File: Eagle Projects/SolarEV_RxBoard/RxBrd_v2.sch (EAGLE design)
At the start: 49 parts, among them U2 ATMEGA32U4-XUAU, X1 USBPTH, X2 5566-6, Y2 16MHz

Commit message: fixed up patels board :D
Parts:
- removed S1: RESET, SparkFun:TAC_SWITCHSMD
- added C10, C11: 100n, resistor:C-USC0805
- added R13, R14, R15, R16: 1k, resistor:R-US_R0805
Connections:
- removed net N$23: ICSP.5, S3.1, S3.2
- new net N$15: R15.1, X2-5.S
- new net RST: ICSP.5, R6.1, S3.1, S3.2, U2.RESET
- net GND: now also C10.2, C11.2, R14.2, R16.2; no longer S1.1, S1.2
- net N$1: now also C11.1, R15.2, R16.1; no longer X2-5.S
- net N$4: now also R13.1; no longer D5.A, D6.C, U2.(PCINT6/OC1B/OC4B/ADC13)PB6
- net N$5: now also C10.1, D5.A, D6.C, R13.2, R14.1, U2.(PCINT6/OC1B/OC4B/ADC13)PB6; no longer R6.1, S1.3, S1.4, U2.RESET
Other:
- moved on the sheet: X2-3, X2-5

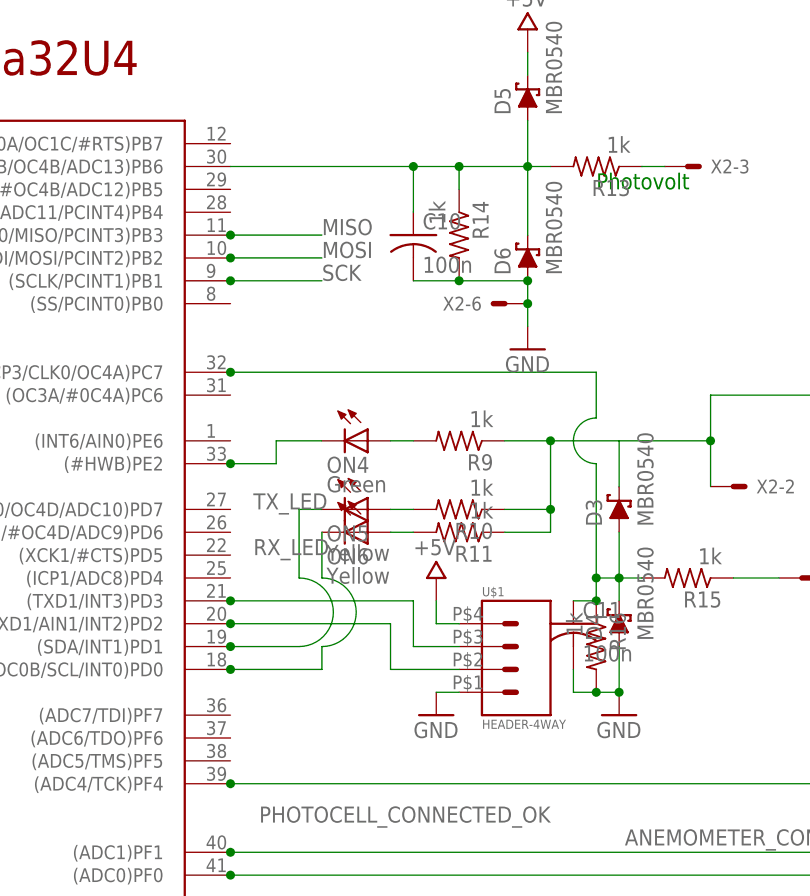
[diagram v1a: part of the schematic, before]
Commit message: final rx board (i think) is still called rev2 xD
on other side, minor software tweaks but they're nonfunctional atm
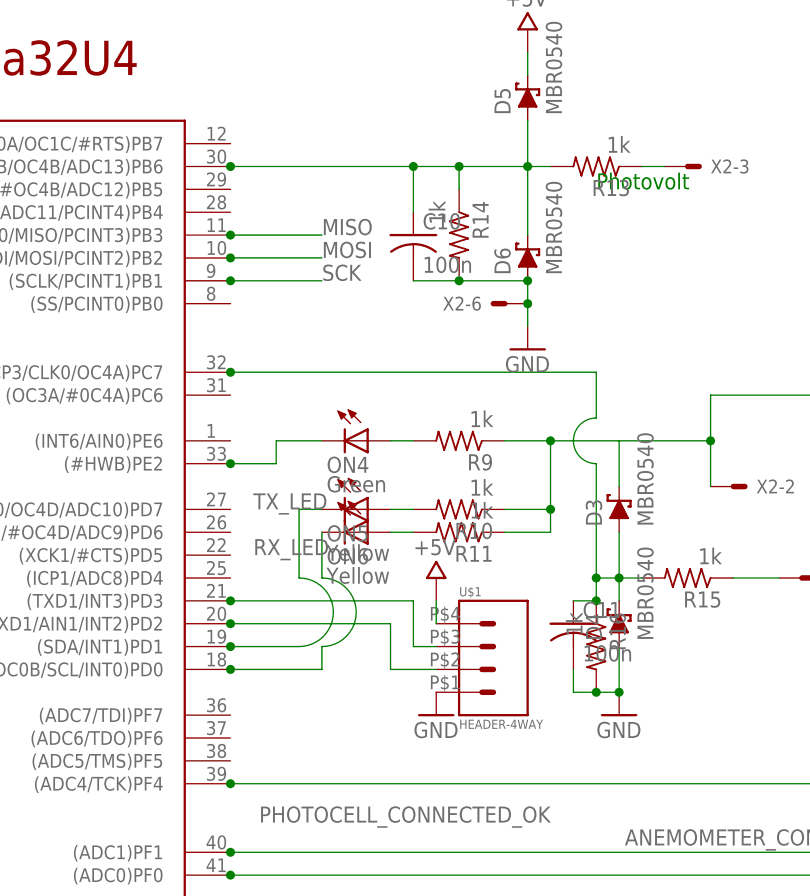
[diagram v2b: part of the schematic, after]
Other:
- moved on the sheet: U$1
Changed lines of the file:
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@@
 <?xml version="1.0" encoding="utf-8"?>
 <!DOCTYPE eagle SYSTEM "eagle.dtd">
-<eagle version="7.2.0">
+<eagle version="7.1.0">
 <drawing>
 <settings>
@@
 <instance part="X2" gate="-6" x="182.88" y="-40.64" rot="R180"/>
 <instance part="JP1" gate="A" x="27.94" y="-30.48"/>
-<instance part="U$1" gate="G$1" x="182.88" y="-78.74"/>
+<instance part="U$1" gate="G$1" x="180.34" y="-78.74"/>
 <instance part="U$3" gate="G$1" x="175.26" y="-71.12"/>
 <instance part="GND10" gate="1" x="175.26" y="-86.36"/>
@@
 <pinref part="U$1" gate="G$1" pin="P$4"/>
 <pinref part="U$3" gate="G$1" pin="+5V"/>
-<wire x1="177.8" y1="-76.2" x2="175.26" y2="-76.2" width="0.1524" layer="91"/>
 <wire x1="175.26" y1="-76.2" x2="175.26" y2="-73.66" width="0.1524" layer="91"/>
 </segment>
@@
 <pinref part="U$1" gate="G$1" pin="P$1"/>
 <pinref part="GND10" gate="1" pin="GND"/>
-<wire x1="177.8" y1="-83.82" x2="175.26" y2="-83.82" width="0.1524" layer="91"/>
 </segment>
 </net>
@@
 <wire x1="170.18" y1="-76.2" x2="170.18" y2="-81.28" width="0.1524" layer="91"/>
 <pinref part="U$1" gate="G$1" pin="P$2"/>
-<wire x1="170.18" y1="-81.28" x2="177.8" y2="-81.28" width="0.1524" layer="91"/>
+<wire x1="170.18" y1="-81.28" x2="175.26" y2="-81.28" width="0.1524" layer="91"/>
 </segment>
 </net>
@@
 <junction x="152.4" y="-73.66"/>
 <pinref part="U$1" gate="G$1" pin="P$3"/>
-<wire x1="177.8" y1="-78.74" x2="172.72" y2="-78.74" width="0.1524" layer="91"/>
+<wire x1="175.26" y1="-78.74" x2="172.72" y2="-78.74" width="0.1524" layer="91"/>
 <wire x1="172.72" y1="-78.74" x2="172.72" y2="-73.66" width="0.1524" layer="91"/>
 </segment>
@@
 <wire x1="172.72" y1="-25.4" x2="172.72" y2="-30.48" width="0.1524" layer="91"/>
 <junction x="172.72" y="-25.4"/>
-</segment>
-</net>
+<junction x="152.4" y="-25.4"/>
+</segment>
+</net>

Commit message: Potato!
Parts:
- removed ICSP: ICSP, SmartPrj:PINHD-2X3
- added Q2: (no value), crystal:CRYSTALHC49S
- JP1: value (none) -> AVR-ISP6-75869-131; device jumper:JP1E -> atmel-avr:AVR-ISP6-75869-131
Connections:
- net GND: now also JP1.6; no longer ICSP.6
- net MISO: now also JP1.1; no longer ICSP.1
- net MOSI: now also JP1.4; no longer ICSP.4
- net N$10: now also JP1.2; no longer ICSP.2
- net RST: now also JP1.5; no longer ICSP.5
- net SCK: now also JP1.3; no longer ICSP.3
- net XTAL1: now also Q2.1
- net XTAL2: now also Q2.2
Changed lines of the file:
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@@
 <?xml version="1.0" encoding="utf-8"?>
 <!DOCTYPE eagle SYSTEM "eagle.dtd">
-<eagle version="7.1.0">
+<eagle version="7.2.0">
 <drawing>
 <settings>
@@
 </classes>
 <parts>
-<part name="ICSP" library="SmartPrj" deviceset="PINHD-2X3" device="" value="ICSP"/>
 <part name="P+1" library="supply1" deviceset="+5V" device=""/>
 <part name="GND12" library="supply1" deviceset="GND" device=""/>
@@
 <part name="X1" library="SparkFun" deviceset="USB" device="PTH"/>
 <part name="X2" library="con-molex" deviceset="5566-6" device=""/>
-<part name="JP1" library="jumper" deviceset="JP1E" device=""/>
 <part name="U$1" library="con-TE-EP" deviceset="HEADER-4WAY" device=""/>
 <part name="U$3" library="MyPOW" deviceset="+5V" device=""/>
@@
 <part name="R16" library="resistor" deviceset="R-US_" device="R0805" value="1k"/>
 <part name="C11" library="resistor" deviceset="C-US" device="C0805" value="100n"/>
+<part name="Q2" library="crystal" deviceset="CRYSTAL" device="HC49S"/>
+<part name="JP1" library="atmel-avr" deviceset="AVR-ISP6-" device="75869-131"/>
 </parts>
 <sheets>
@@
 </plain>
 <instances>
-<instance part="ICSP" gate="A" x="71.12" y="-96.52" smashed="yes">
-<attribute name="NAME" x="64.77" y="-90.805" size="1.778" layer="95"/>
-<attribute name="VALUE" x="74.93" y="-91.44" size="1.778" layer="96"/>
-</instance>
 <instance part="P+1" gate="1" x="86.36" y="-83.82" smashed="yes">
 <attribute name="VALUE" x="88.265" y="-81.28" size="1.778" layer="96" rot="R180"/>
@@
 <instance part="X2" gate="-5" x="215.9" y="-71.12"/>
 <instance part="X2" gate="-6" x="182.88" y="-40.64" rot="R180"/>
-<instance part="JP1" gate="A" x="27.94" y="-30.48"/>
 <instance part="U$1" gate="G$1" x="180.34" y="-78.74"/>
 <instance part="U$3" gate="G$1" x="175.26" y="-71.12"/>
@@
 <instance part="R16" gate="G$1" x="193.04" y="-78.74" rot="R270"/>
 <instance part="C11" gate="G$1" x="190.5" y="-76.2"/>
+<instance part="Q2" gate="G$1" x="71.12" y="-33.02" rot="R90"/>
+<instance part="JP1" gate="G$1" x="78.74" y="-134.62" rot="R90"/>
 </instances>
 <busses>
@@
 <segment>
 <wire x1="86.36" y1="-99.06" x2="76.2" y2="-99.06" width="0.1524" layer="91"/>
-<pinref part="ICSP" gate="A" pin="6"/>
 <pinref part="GND1" gate="1" pin="GND"/>
-<junction x="76.2" y="-99.06"/>
 </segment>
 <segment>
@@
 <pinref part="GND10" gate="1" pin="GND"/>
 </segment>
+<segment>
+<pinref part="JP1" gate="G$1" pin="6"/>
+<wire x1="86.36" y1="-127" x2="86.36" y2="-116.84" width="0.1524" layer="91"/>
+<label x="86.36" y="-116.84" size="1.778" layer="95" rot="R90"/>
+</segment>
 </net>
 <net name="AREF" class="4">
@@
 <wire x1="68.58" y1="-96.52" x2="58.42" y2="-96.52" width="0.1524" layer="91"/>
 <label x="53.34" y="-96.52" size="1.778" layer="95"/>
-<pinref part="ICSP" gate="A" pin="3"/>
-<junction x="68.58" y="-96.52"/>
+</segment>
+<segment>
+<pinref part="JP1" gate="G$1" pin="3"/>
+<wire x1="78.74" y1="-127" x2="78.74" y2="-116.84" width="0.1524" layer="91"/>
+<label x="78.74" y="-116.84" size="1.778" layer="95" rot="R90"/>
 </segment>
 </net>
@@
 <wire x1="68.58" y1="-93.98" x2="60.96" y2="-93.98" width="0.1524" layer="91"/>
 <label x="55.88" y="-93.98" size="1.778" layer="95"/>
-<pinref part="ICSP" gate="A" pin="1"/>
-<junction x="68.58" y="-93.98"/>
+</segment>
+<segment>
+<pinref part="JP1" gate="G$1" pin="1"/>
+<wire x1="73.66" y1="-127" x2="73.66" y2="-116.84" width="0.1524" layer="91"/>
+<label x="73.66" y="-116.84" size="1.778" layer="95" rot="R90"/>
 </segment>
 </net>
@@
 <wire x1="76.2" y1="-96.52" x2="86.36" y2="-96.52" width="0.1524" layer="91"/>
 <label x="81.28" y="-96.52" size="1.778" layer="95"/>
-<pinref part="ICSP" gate="A" pin="4"/>
-<junction x="76.2" y="-96.52"/>
+</segment>
+<segment>
+<pinref part="JP1" gate="G$1" pin="4"/>
+<wire x1="81.28" y1="-127" x2="81.28" y2="-116.84" width="0.1524" layer="91"/>
+<label x="81.28" y="-116.84" size="1.778" layer="95" rot="R90"/>
 </segment>
 </net>
@@
 <wire x1="78.74" y1="-35.56" x2="71.12" y2="-27.94" width="0.1524" layer="91"/>
 <junction x="91.44" y="-35.56"/>
+<pinref part="Q2" gate="G$1" pin="2"/>
+<wire x1="71.12" y1="-27.94" x2="71.12" y2="-30.48" width="0.1524" layer="91"/>
+<junction x="71.12" y="-27.94"/>
 </segment>
 </net>
@@
 <wire x1="73.66" y1="-40.64" x2="71.12" y2="-38.1" width="0.1524" layer="91"/>
 <junction x="91.44" y="-40.64"/>
+<pinref part="Q2" gate="G$1" pin="1"/>
+<wire x1="71.12" y1="-38.1" x2="71.12" y2="-35.56" width="0.1524" layer="91"/>
+<junction x="71.12" y="-38.1"/>
 </segment>
 </net>
@@
 <net name="N$10" class="3">
 <segment>
-<wire x1="86.36" y1="-93.98" x2="76.2" y2="-93.98" width="0.1524" layer="91"/>
-<pinref part="ICSP" gate="A" pin="2"/>
+<wire x1="86.36" y1="-93.98" x2="73.66" y2="-93.98" width="0.1524" layer="91"/>
 <pinref part="D2" gate="G$1" pin="A"/>
-<junction x="76.2" y="-93.98"/>
+<wire x1="73.66" y1="-93.98" x2="73.66" y2="-109.22" width="0.1524" layer="91"/>
+<wire x1="73.66" y1="-109.22" x2="76.2" y2="-109.22" width="0.1524" layer="91"/>
+<pinref part="JP1" gate="G$1" pin="2"/>
+<wire x1="76.2" y1="-109.22" x2="76.2" y2="-127" width="0.1524" layer="91"/>
 </segment>
 </net>
@@
 </segment>
 <segment>
-<pinref part="ICSP" gate="A" pin="5"/>
 <wire x1="68.58" y1="-99.06" x2="60.96" y2="-99.06" width="0.1524" layer="91"/>
 <pinref part="S3" gate="S" pin="2"/>
@@
 <wire x1="55.88" y1="-101.6" x2="58.42" y2="-101.6" width="0.1524" layer="91"/>
 <wire x1="58.42" y1="-101.6" x2="58.42" y2="-99.06" width="0.1524" layer="91"/>
-<junction x="68.58" y="-99.06"/>
 <wire x1="60.96" y1="-99.06" x2="60.96" y2="-106.68" width="0.1524" layer="91"/>
 <junction x="60.96" y="-99.06"/>
 <label x="63.5" y="-109.22" size="1.778" layer="95"/>
 </segment>
-</net>
+<segment>
+<pinref part="JP1" gate="G$1" pin="5"/>
+<wire x1="83.82" y1="-127" x2="83.82" y2="-116.84" width="0.1524" layer="91"/>
+<label x="83.82" y="-116.84" size="1.778" layer="95" rot="R90"/>
+</segment>
+</net>

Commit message: Fixed patties board
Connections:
- net GND: now also U2.(#HWB)PE2
- net N$13: now also U2.(OC3A/#0C4A)PC6; no longer U2.(#HWB)PE2
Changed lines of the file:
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@@
 <part name="Q2" library="crystal" deviceset="CRYSTAL" device="HC49S"/>
 <part name="JP1" library="atmel-avr" deviceset="AVR-ISP6-" device="75869-131"/>
+<part name="GND6" library="supply1" deviceset="GND" device=""/>
 </parts>
 <sheets>
@@
 <instance part="Q2" gate="G$1" x="71.12" y="-33.02" rot="R90"/>
 <instance part="JP1" gate="G$1" x="78.74" y="-134.62" rot="R90"/>
+<instance part="GND6" gate="1" x="154.94" y="-60.96"/>
 </instances>
 <busses>
@@
 <label x="86.36" y="-116.84" size="1.778" layer="95" rot="R90"/>
 </segment>
+<segment>
+<pinref part="U2" gate="G$1" pin="(#HWB)PE2"/>
+<pinref part="GND6" gate="1" pin="GND"/>
+<wire x1="152.4" y1="-58.42" x2="154.94" y2="-58.42" width="0.1524" layer="91"/>
+</segment>
 </net>
 <net name="AREF" class="4">
@@
 <net name="N$13" class="0">
 <segment>
-<pinref part="U2" gate="G$1" pin="(#HWB)PE2"/>
-<wire x1="152.4" y1="-58.42" x2="157.48" y2="-58.42" width="0.1524" layer="91"/>
-<wire x1="157.48" y1="-58.42" x2="157.48" y2="-55.88" width="0.1524" layer="91"/>
 <pinref part="ON4" gate="G$1" pin="C"/>
 <wire x1="157.48" y1="-55.88" x2="162.56" y2="-55.88" width="0.1524" layer="91"/>
-<junction x="152.4" y="-58.42"/>
-</segment>
-</net>
+<pinref part="U2" gate="G$1" pin="(OC3A/#0C4A)PC6"/>
+<wire x1="152.4" y1="-50.8" x2="157.48" y2="-50.8" width="0.1524" layer="91"/>
+<wire x1="157.48" y1="-50.8" x2="157.48" y2="-55.88" width="0.1524" layer="91"/>
+</segment>
+</net>
